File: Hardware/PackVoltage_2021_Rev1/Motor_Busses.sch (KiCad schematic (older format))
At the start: 50 parts, among them Q1 Q_NMOS_DGS, Q2 Q_NMOS_DGS, Q3 Q_NMOS_DGS, Q4 Q_NMOS_DGS, Q9 Q_NMOS_DGS, U2 LT1910, U21 LT1910, U22 INA281, U3 LT1910, U4 LT1910, U5 INA281, U6 INA281, U7 INA281, U8 LT1910, U9 INA281

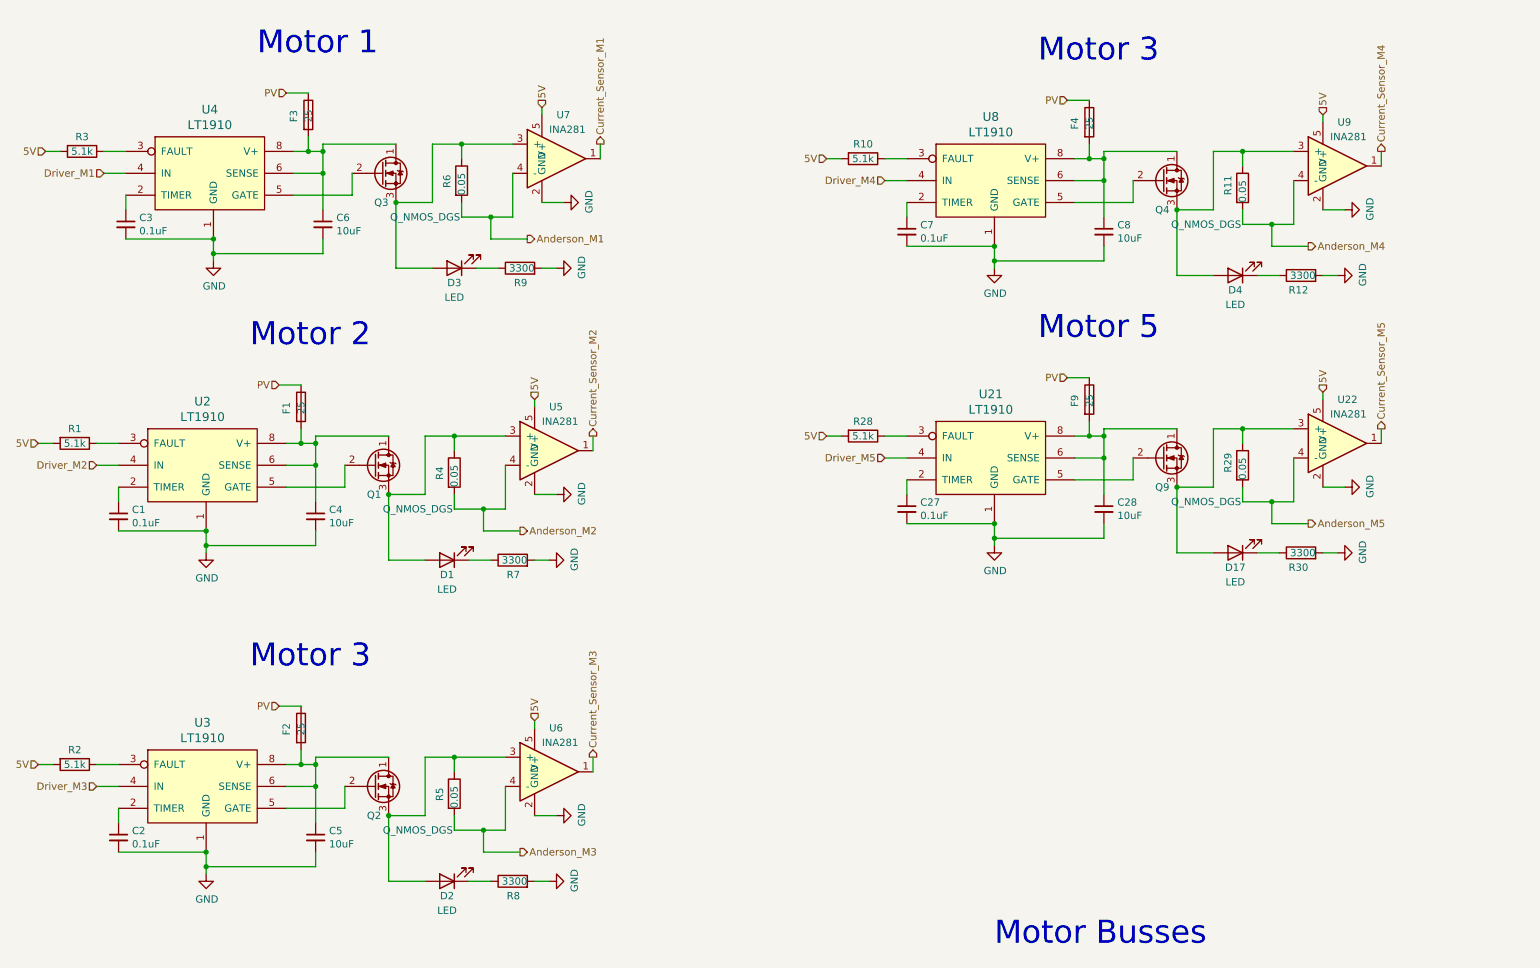
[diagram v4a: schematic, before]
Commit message: updated busses, fuses, and some names
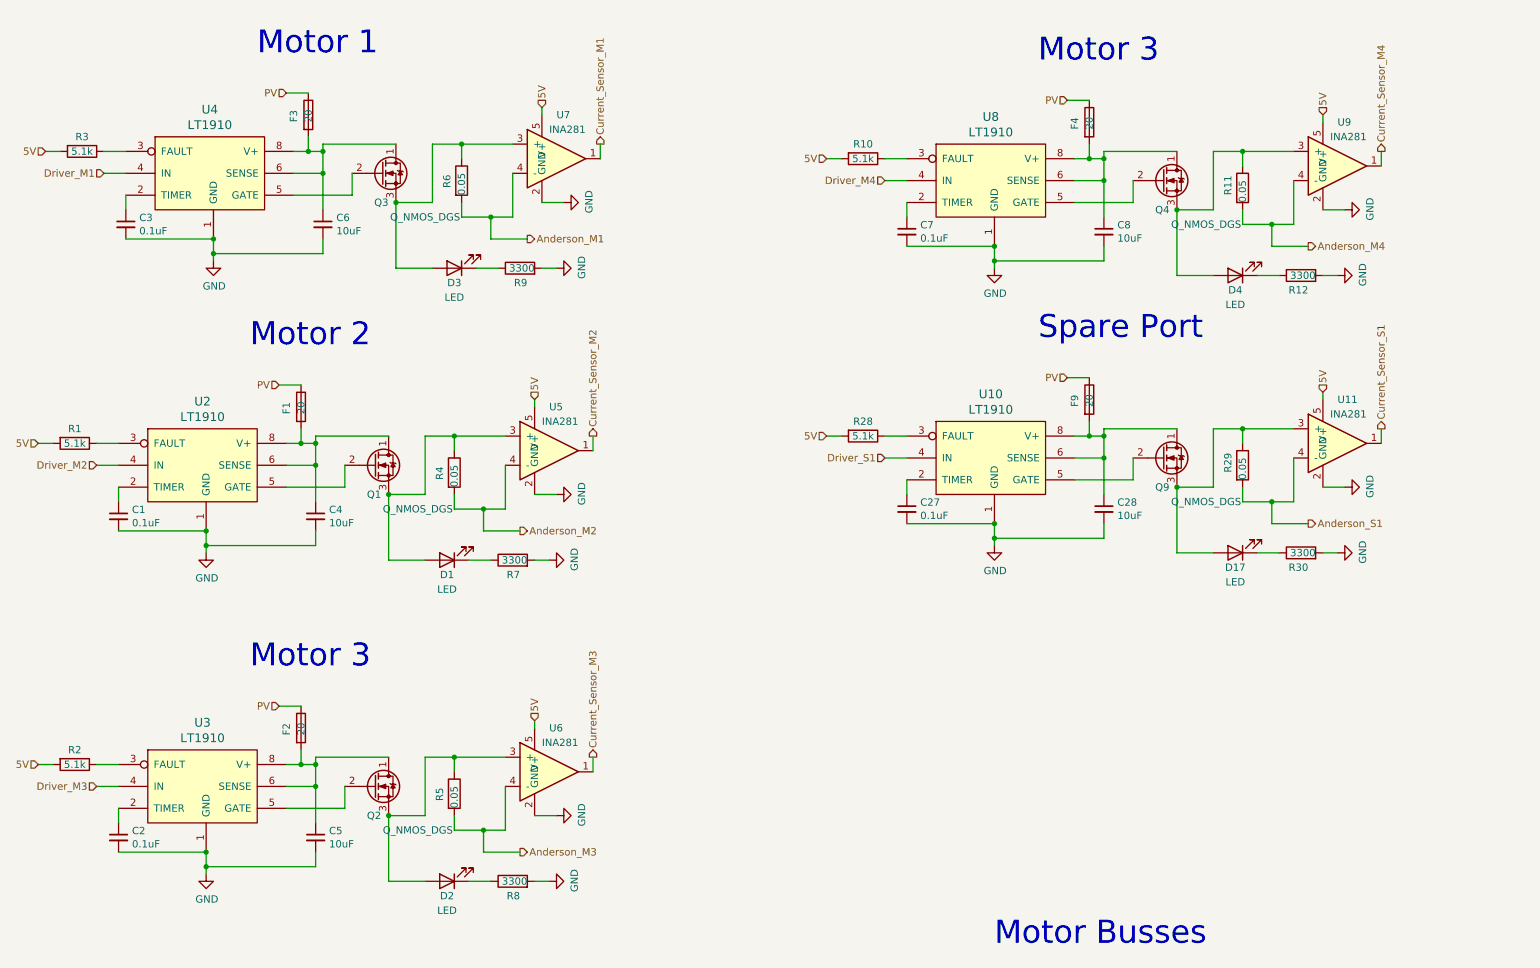
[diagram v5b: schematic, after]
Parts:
- F1, F2, F3, F4, F9: value 25 -> 20
- renumbered U21 to U10, U22 to U11
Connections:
- net Anderson_M5 renamed Anderson_S1
- net Current_Sensor_M5 renamed Current_Sensor_S1
- net Driver_M5 renamed Driver_S1
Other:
- note added: "Spare Port"
- note removed: "Motor 5"
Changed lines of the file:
@@
 $Descr A4 11693 8268
 encoding utf-8
-Sheet 3 5
+Sheet 2 5
 Title ""
 Date ""
@@
 AR Path="/5F8EFCC9/5F9AF78C" Ref="F?"  Part="1"
 F 0 "F3" V 2400 1200 50  0000 L CNN
-F 1 "25" V 2500 1200 50  0000 L CNN
+F 1 "20" V 2500 1200 50  0000 L CNN
 F 2 "" V 2430 1250 50  0001 C CNN
 F 3 "~" H 2500 1250 50  0001 C CNN
@@
 AR Path="/5F8EFCC9/5F89ED83" Ref="F?"  Part="1"
 F 0 "F1" V 2350 3200 50  0000 L CNN
-F 1 "25" V 2450 3200 50  0000 L CNN
+F 1 "20" V 2450 3200 50  0000 L CNN
 F 2 "" V 2380 3250 50  0001 C CNN
 F 3 "~" H 2450 3250 50  0001 C CNN
@@
 AR Path="/5F8EFCC9/5F9AF7A3" Ref="F?"  Part="1"
 F 0 "F2" V 2350 5400 50  0000 L CNN
-F 1 "25" V 2450 5400 50  0000 L CNN
+F 1 "20" V 2450 5400 50  0000 L CNN
 F 2 "" V 2380 5450 50  0001 C CNN
 F 3 "~" H 2450 5450 50  0001 C CNN
@@
 AR Path="/5F8EFCC9/5F9AF7B0" Ref="F?"  Part="1"
 F 0 "F4" V 7750 1250 50  0000 L CNN
-F 1 "25" V 7850 1250 50  0000 L CNN
+F 1 "20" V 7850 1250 50  0000 L CNN
 F 2 "" V 7780 1300 50  0001 C CNN
 F 3 "~" H 7850 1300 50  0001 C CNN
@@
 AR Path="/5F8EFCC9/5F880754" Ref="F?"  Part="1"
 F 0 "F9" V 7750 3150 50  0000 L CNN
-F 1 "25" V 7850 3150 50  0000 L CNN
+F 1 "20" V 7850 3150 50  0000 L CNN
 F 2 "" V 7780 3200 50  0001 C CNN
 F 3 "~" H 7850 3200 50  0001 C CNN
@@
 Connection ~ 7950 3450
 Text Notes 7500 2800 0    157  ~ 0
-Motor 5
+Spare Port
 Wire Wire Line
 	8700 3800 8700 3400
@@
 PV
 $Comp
-L MRDT_ICs:INA281 U22
+L MRDT_ICs:INA281 U11
 U 1 1 5F8807A7
 P 9450 3500
-AR Path="/5F7A6A8B/5F8807A7" Ref="U22"  Part="1"
+AR Path="/5F7A6A8B/5F8807A7" Ref="U11"  Part="1"
 AR Path="/5F8EFCC9/5F8807A7" Ref="U?"  Part="1"
-F 0 "U22" H 9550 3800 50  0000 L CNN
+F 0 "U11" H 9550 3800 50  0000 L CNN
 F 1 "INA281" H 9500 3700 50  0000 L CNN
 F 2 "" H 9700 3700 50  0001 C CNN
@@
 $EndComp
 $Comp
-L MRDT_ICs:LT1910 U21
+L MRDT_ICs:LT1910 U10
 U 1 1 5F8807AD
 P 6800 3850
-AR Path="/5F7A6A8B/5F8807AD" Ref="U21"  Part="1"
+AR Path="/5F7A6A8B/5F8807AD" Ref="U10"  Part="1"
 AR Path="/5F8EFCC9/5F8807AD" Ref="U?"  Part="1"
-F 0 "U21" H 7175 4537 60  0000 C CNN
+F 0 "U10" H 7175 4537 60  0000 C CNN
 F 1 "LT1910" H 7175 4431 60  0000 C CNN
 F 2 "" H 6800 3850 60  0001 C CNN
@@
 	9850 3500 9850 3400
 Text HLabel 6450 3600 0    50   Input ~ 0
-Driver_M5
+Driver_S1
 Wire Wire Line
 	8450 3800 8700 3800
@@
 	9100 4050 9350 4050
 Text HLabel 9850 3400 1    50   Output ~ 0
-Current_Sensor_M5
+Current_Sensor_S1
 Text HLabel 9350 4050 2    50   Output ~ 0
-Anderson_M5
+Anderson_S1
 Wire Wire Line
 	3100 1850 3100 2300

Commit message: corrected orientation of ground symbols, renamed buck converters, still need to update tiva with extra 12V pin
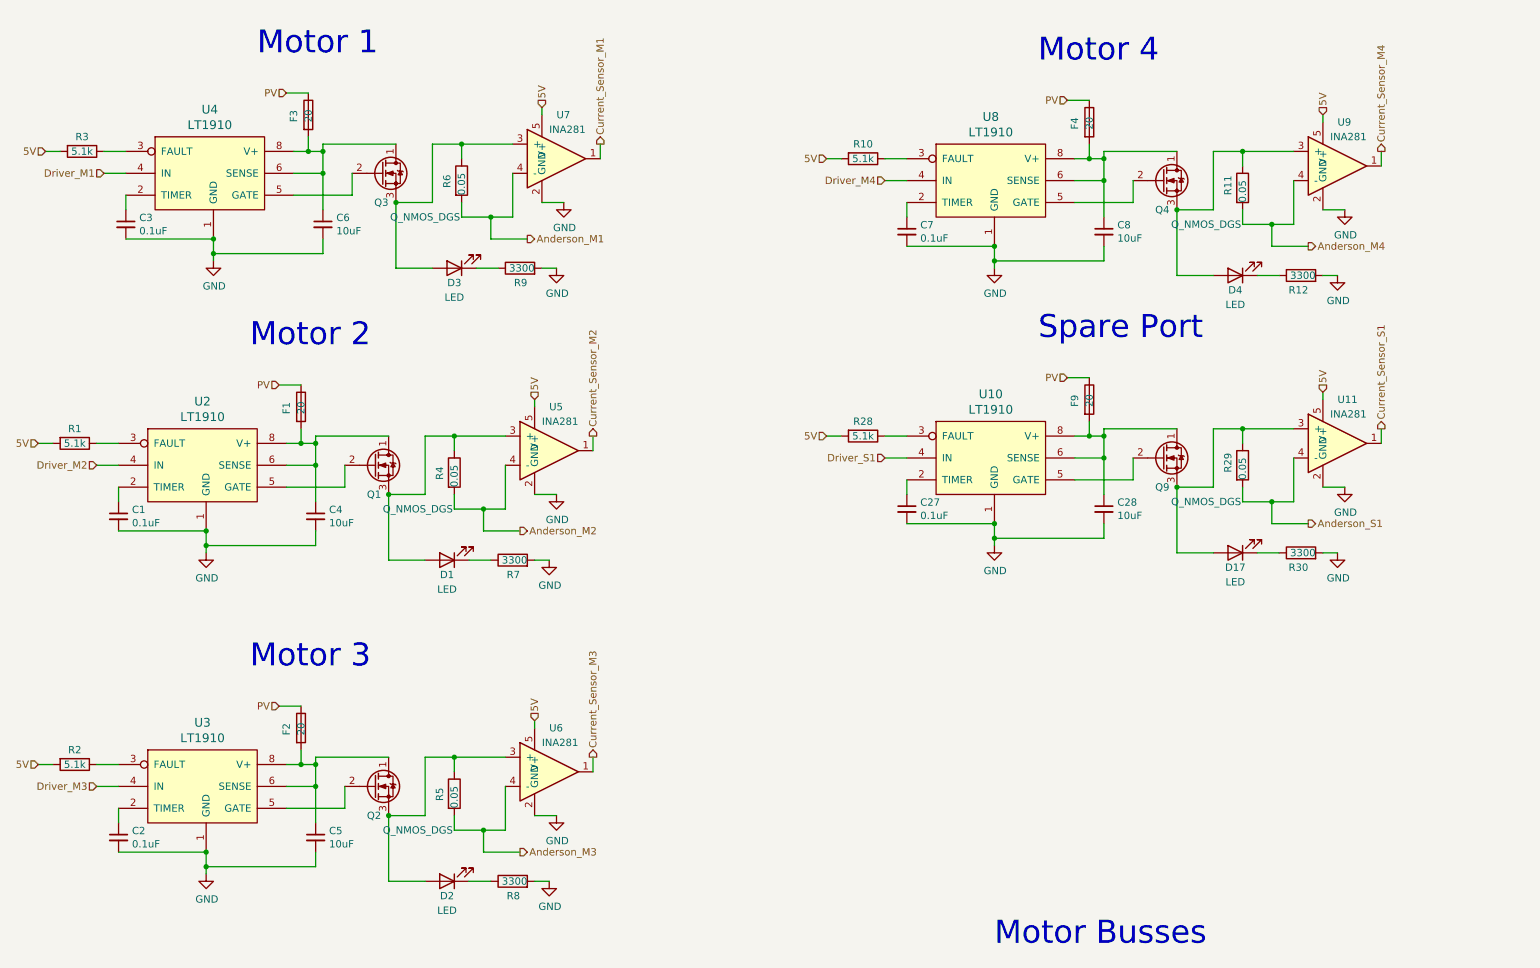
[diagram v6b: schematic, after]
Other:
- note added: "Motor 4"
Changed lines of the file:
@@
 F 3 "" H 4250 1850 50  0001 C CNN
 	1    4250 1850
-	0    -1   -1   0
+	1    0    0    -1
 $EndComp
 $Comp
@@
 F 3 "" H 4200 2300 50  0001 C CNN
 	1    4200 2300
-	0    -1   -1   0
+	1    0    0    -1
 $EndComp
 Connection ~ 3100 1850
@@
 F 3 "" H 4200 3850 50  0001 C CNN
 	1    4200 3850
-	0    -1   -1   0
+	1    0    0    -1
 $EndComp
 $Comp
@@
 F 3 "" H 4150 4300 50  0001 C CNN
 	1    4150 4300
-	0    -1   -1   0
+	1    0    0    -1
 $EndComp
 Connection ~ 3050 3850
@@
 F 3 "" H 4200 6050 50  0001 C CNN
 	1    4200 6050
-	0    -1   -1   0
+	1    0    0    -1
 $EndComp
 $Comp
@@
 F 3 "" H 4150 6500 50  0001 C CNN
 	1    4150 6500
-	0    -1   -1   0
+	1    0    0    -1
 $EndComp
 Connection ~ 3050 6050
@@
 Connection ~ 7950 1550
 Text Notes 7500 900  0    157  ~ 0
-Motor 3
+Motor 4
 Wire Wire Line
 	8700 1900 8700 1500
@@
 F 3 "" H 9600 1900 50  0001 C CNN
 	1    9600 1900
-	0    -1   -1   0
+	1    0    0    -1
 $EndComp
 $Comp
@@
 F 3 "" H 9550 2350 50  0001 C CNN
 	1    9550 2350
-	0    -1   -1   0
+	1    0    0    -1
 $EndComp
 Connection ~ 8450 1900
@@
 F 3 "" H 9600 3800 50  0001 C CNN
 	1    9600 3800
-	0    -1   -1   0
+	1    0    0    -1
 $EndComp
 $Comp
@@
 F 3 "" H 9550 4250 50  0001 C CNN
 	1    9550 4250
-	0    -1   -1   0
+	1    0    0    -1
 $EndComp
 Connection ~ 8450 3800

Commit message: Updated molex connector (Still need tiva pin)
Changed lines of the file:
@@
 Wire Wire Line
 	4100 2300 4200 2300
-Text HLabel 2350 1100 0    50   Input ~ 0
+Text HLabel 2350 1100 1    50   Input ~ 0
 PV
 $Comp
@@
 Text HLabel 4100 1200 1    50   Input ~ 0
 5V
-Text HLabel 700  1500 0    50   Input ~ 0
-5V
 Wire Wire Line
 	700  1500 800  1500
 Wire Wire Line
 	4100 1200 4100 1250
-Wire Wire Line
-	4500 1550 4500 1450
 Text HLabel 1100 1650 0    50   Input ~ 0
 Driver_M1
@@
 Wire Wire Line
 	3750 2100 4000 2100
-Text HLabel 4500 1450 1    50   Output ~ 0
+Text HLabel 4600 1550 2    50   Output ~ 0
 Current_Sensor_M1
 $Comp
@@
 Wire Wire Line
 	4050 4300 4150 4300
-Text HLabel 2300 3100 0    50   Input ~ 0
+Text HLabel 2300 3100 1    50   Input ~ 0
 PV
 $Comp
@@
 Text HLabel 4050 3200 1    50   Input ~ 0
 5V
-Text HLabel 650  3500 0    50   Input ~ 0
-5V
 Wire Wire Line
 	650  3500 750  3500
 Wire Wire Line
 	4050 3200 4050 3250
-Wire Wire Line
-	4450 3550 4450 3450
 Text HLabel 1050 3650 0    50   Input ~ 0
 Driver_M2
@@
 Wire Wire Line
 	3700 4100 3950 4100
-Text HLabel 4450 3450 1    50   Output ~ 0
+Text HLabel 4550 3550 2    50   Output ~ 0
 Current_Sensor_M2
 $Comp
@@
 Wire Wire Line
 	4050 6500 4150 6500
-Text HLabel 2300 5300 0    50   Input ~ 0
+Text HLabel 2300 5300 1    50   Input ~ 0
 PV
 $Comp
@@
 Text HLabel 4050 5400 1    50   Input ~ 0
 5V
-Text HLabel 650  5700 0    50   Input ~ 0
-5V
 Wire Wire Line
 	650  5700 750  5700
 Wire Wire Line
 	4050 5400 4050 5450
-Wire Wire Line
-	4450 5750 4450 5650
 Text HLabel 1050 5850 0    50   Input ~ 0
 Driver_M3
@@
 Wire Wire Line
 	3700 6300 3950 6300
-Text HLabel 4450 5650 1    50   Output ~ 0
+Text HLabel 4550 5750 2    50   Output ~ 0
 Current_Sensor_M3
 $Comp
@@
 Wire Wire Line
 	9450 2350 9550 2350
-Text HLabel 7700 1150 0    50   Input ~ 0
+Text HLabel 7700 1150 1    50   Input ~ 0
 PV
 $Comp
@@
 Text HLabel 9450 1250 1    50   Input ~ 0
 5V
-Text HLabel 6050 1550 0    50   Input ~ 0
-5V
 Wire Wire Line
 	6050 1550 6150 1550
 Wire Wire Line
 	9450 1250 9450 1300
-Wire Wire Line
-	9850 1600 9850 1500
 Text HLabel 6450 1700 0    50   Input ~ 0
 Driver_M4
@@
 Wire Wire Line
 	9100 2150 9350 2150
-Text HLabel 9850 1500 1    50   Output ~ 0
-Current_Sensor_M4
 Text HLabel 4000 2100 2    50   Output ~ 0
 Anderson_M1
@@
 Wire Wire Line
 	9450 4250 9550 4250
-Text HLabel 7700 3050 0    50   Input ~ 0
+Text HLabel 7700 3050 1    50   Input ~ 0
 PV
 $Comp
@@
 Text HLabel 9450 3150 1    50   Input ~ 0
 5V
-Text HLabel 6050 3450 0    50   Input ~ 0
+Text HLabel 6050 3100 1    50   Input ~ 0
 5V
 Wire Wire Line
@@
 Wire Wire Line
 	9450 3150 9450 3200
-Wire Wire Line
-	9850 3500 9850 3400
 Text HLabel 6450 3600 0    50   Input ~ 0
 Driver_S1
@@
 Wire Wire Line
 	9100 4050 9350 4050
-Text HLabel 9850 3400 1    50   Output ~ 0
+Text HLabel 9950 3500 2    50   Output ~ 0
 Current_Sensor_S1
 Text HLabel 9350 4050 2    50   Output ~ 0
@@
 Wire Wire Line
 	9100 2000 9250 2000
+Text HLabel 9950 1600 2    50   Output ~ 0
+Current_Sensor_M4
+Wire Wire Line
+	4450 5750 4550 5750
+Wire Wire Line
+	4450 3550 4550 3550
+Wire Wire Line
+	4600 1550 4500 1550
+Wire Wire Line
+	9850 3500 9950 3500
+Wire Wire Line
+	9850 1600 9950 1600
+Wire Wire Line
+	6050 3100 6050 3450
+Text HLabel 6050 1200 1    50   Input ~ 0
+5V
+Wire Wire Line
+	6050 1200 6050 1550
+Text HLabel 700  1150 1    50   Input ~ 0
+5V
+Wire Wire Line
+	700  1150 700  1500
+Text HLabel 650  3150 1    50   Input ~ 0
+5V
+Wire Wire Line
+	650  3150 650  3500
+Text HLabel 650  5350 1    50   Input ~ 0
+5V
+Wire Wire Line
+	650  5350 650  5700
 $EndSCHEMATC
